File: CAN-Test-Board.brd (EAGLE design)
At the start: 52.3 x 59.4 mm, 52 parts, among them Y1 ECS-80-S-4X, Y2 ECS-80-S-4X

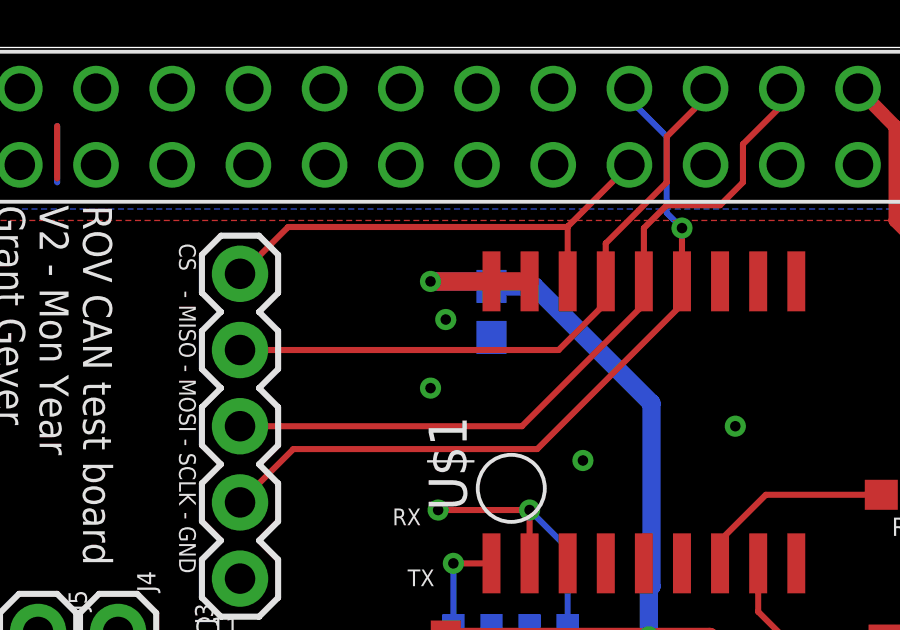
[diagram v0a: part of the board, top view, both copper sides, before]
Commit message: Add missing interrupt connection
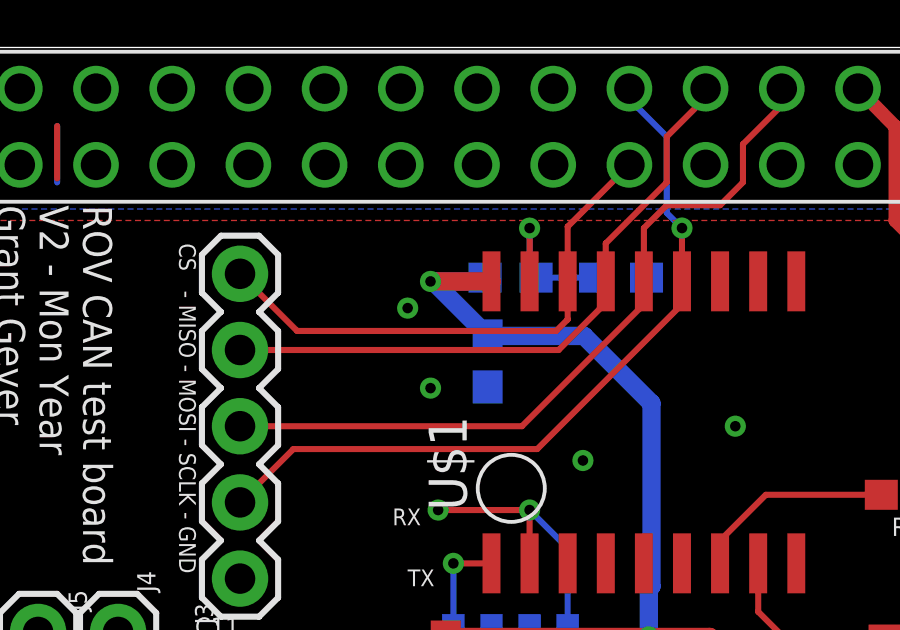
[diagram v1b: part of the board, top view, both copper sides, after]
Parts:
- added C19: 0.1uF, SparkFun-Capacitors:0603
- added R16: 10k, SparkFun-Resistors:0603
- C7: value 4.7uF -> 0.1uF
- R2: value 1k -> 10k
- moved C12 1.66 mm to (17.7, 48.9)
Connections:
- new net MCP_RESET: C19.2, R16.1, U$1.RESET
- net 3V3: now also R16.2; no longer U$1.RESET
- net GND: now also C19.1
- net INT: now also PCB1.P$37
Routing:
- net MCP_RESET: track 0.00 -> 5.50 mm, vias 0 -> 1
- net CS: track 16.3 -> 17.9 mm
- net 3V3: track 171.3 -> 171.9 mm
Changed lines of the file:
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@@
 <?xml version="1.0" encoding="utf-8"?>
 <!DOCTYPE eagle SYSTEM "eagle.dtd">
-<eagle version="9.6.2">
+<eagle version="9.6.0">
 <drawing>
 <settings>
@@
 <attribute name="VALUE" x="8.636" y="38.227" size="0.6096" layer="27" font="vector" ratio="20" align="top-center"/>
 </element>
-<element name="C12" library="SparkFun-Capacitors" library_urn="urn:adsk.eagle:library:510" package="0603" package3d_urn="urn:adsk.eagle:package:37414@1/1" value="0.1uF" x="17.78" y="50.546" smashed="yes" rot="MR90">
-<attribute name="NAME" x="18.542" y="50.546" size="0.6096" layer="26" font="vector" ratio="20" rot="MR90" align="bottom-center"/>
-<attribute name="PROD_ID" value="CAP-07885" x="-69.85" y="147.066" size="1.778" layer="28" rot="MR90" display="off"/>
-<attribute name="VALUE" x="17.018" y="50.546" size="0.6096" layer="28" font="vector" ratio="20" rot="MR90" align="top-center"/>
+<element name="C12" library="SparkFun-Capacitors" library_urn="urn:adsk.eagle:library:510" package="0603" package3d_urn="urn:adsk.eagle:package:37414@1/1" value="0.1uF" x="17.653" y="48.895" smashed="yes" rot="MR90">
+<attribute name="NAME" x="18.415" y="48.895" size="0.6096" layer="26" font="vector" ratio="20" rot="MR90" align="bottom-center"/>
+<attribute name="PROD_ID" value="CAP-07885" x="-69.977" y="145.415" size="1.778" layer="28" rot="MR90" display="off"/>
+<attribute name="VALUE" x="16.891" y="48.895" size="0.6096" layer="28" font="vector" ratio="20" rot="MR90" align="top-center"/>
 </element>
 <element name="C15" library="SparkFun-Capacitors" library_urn="urn:adsk.eagle:library:510" package="0603" package3d_urn="urn:adsk.eagle:package:37414@1/1" value="0.1uF" x="22.606" y="37.592" smashed="yes" rot="MR90">
@@
 <attribute name="VALUE" x="16.002" y="17.526" size="0.6096" layer="28" font="vector" ratio="20" rot="MR90" align="top-center"/>
 </element>
-<element name="C7" library="SparkFun-Capacitors" library_urn="urn:adsk.eagle:library:510" package="0603" package3d_urn="urn:adsk.eagle:package:37414@2/1" value="4.7uF" x="21.336" y="8.636" smashed="yes" rot="MR180">
+<element name="C7" library="SparkFun-Capacitors" library_urn="urn:adsk.eagle:library:510" package="0603" package3d_urn="urn:adsk.eagle:package:37414@2/1" value="0.1uF" x="21.336" y="8.636" smashed="yes" rot="MR180">
 <attribute name="NAME" x="21.336" y="7.874" size="0.6096" layer="26" font="vector" ratio="20" rot="MR180" align="bottom-center"/>
 <attribute name="PROD_ID" value="CAP-08280" x="98.806" y="96.266" size="1.778" layer="28" rot="MR180" display="off"/>
@@
 <attribute name="VALUE" x="31.75" y="40.386" size="0.6096" layer="27" font="vector" ratio="20" rot="R180" align="top-center"/>
 </element>
-<element name="R2" library="SparkFun-Resistors" library_urn="urn:adsk.eagle:library:532" package="0603" package3d_urn="urn:adsk.eagle:package:39650/1" value="1k" x="20.574" y="5.842" smashed="yes" rot="MR270">
+<element name="R2" library="SparkFun-Resistors" library_urn="urn:adsk.eagle:library:532" package="0603" package3d_urn="urn:adsk.eagle:package:39650/1" value="10k" x="20.574" y="5.842" smashed="yes" rot="MR270">
 <attribute name="NAME" x="19.812" y="5.842" size="0.6096" layer="26" font="vector" ratio="20" rot="MR270" align="bottom-center"/>
 <attribute name="PROD_ID" value="RES-07856" x="113.284" y="-28.448" size="1.778" layer="28" rot="MR270" display="off"/>
@@
 <attribute name="NAME" x="12.954" y="9.906" size="1.27" layer="25"/>
 <attribute name="VALUE" x="12.954" y="4.826" size="1.27" layer="27"/>
+</element>
+<element name="C19" library="SparkFun-Capacitors" library_urn="urn:adsk.eagle:library:510" package="0603" package3d_urn="urn:adsk.eagle:package:37414@1/1" value="0.1uF" x="22.098" y="51.689" smashed="yes" rot="MR0">
+<attribute name="NAME" x="22.098" y="52.451" size="0.6096" layer="26" font="vector" ratio="20" rot="MR0" align="bottom-center"/>
+<attribute name="PROD_ID" value="CAP-07885" x="22.098" y="51.689" size="1.778" layer="28" rot="MR0" display="off"/>
+<attribute name="VALUE" x="22.098" y="50.927" size="0.6096" layer="28" font="vector" ratio="20" rot="MR0" align="top-center"/>
+</element>
+<element name="R16" library="SparkFun-Resistors" library_urn="urn:adsk.eagle:library:532" package="0603" package3d_urn="urn:adsk.eagle:package:39650/1" value="10k" x="18.415" y="51.689" smashed="yes" rot="MR0">
+<attribute name="NAME" x="18.415" y="52.451" size="0.6096" layer="26" font="vector" ratio="20" rot="MR0" align="bottom-center"/>
+<attribute name="PROD_ID" value="RES-07856" x="18.288" y="51.689" size="1.778" layer="28" rot="MR0" display="off"/>
+<attribute name="VALUE" x="18.415" y="50.927" size="0.6096" layer="28" font="vector" ratio="20" rot="MR0" align="top-center"/>
 </element>
 </elements>
@@
 <via x="3.937" y="32.512" extent="1-16" drill="0.35"/>
 <via x="8.89" y="32.893" extent="1-16" drill="0.35"/>
-<via x="16.256" y="50.292" extent="1-16" drill="0.35"/>
+<via x="14.986" y="50.673" extent="1-16" drill="0.35"/>
 <via x="15.748" y="48.006" extent="1-16" drill="0.35"/>
 <via x="20.828" y="45.593" extent="1-16" drill="0.35"/>
@@
 <via x="37.338" y="53.086" extent="1-16" drill="0.35"/>
 <contactref element="RESET" pad="1"/>
+<contactref element="C19" pad="1"/>
 </signal>
 <signal name="CAN_H" class="1">
@@
 <wire x1="22.3774" y1="55.4482" x2="20.32" y2="53.3908" width="0.2032" layer="1"/>
 <wire x1="20.32" y1="53.3908" x2="20.32" y2="51.564" width="0.2032" layer="1"/>
-<wire x1="20.32" y1="53.3908" x2="20.306" y2="53.3768" width="0.2032" layer="1"/>
-<wire x1="9.44295" y1="51.816" x2="9.398" y2="51.816" width="0.2032" layer="1"/>
-<wire x1="11.00375" y1="53.3768" x2="9.44295" y2="51.816" width="0.2032" layer="1"/>
-<wire x1="20.306" y1="53.3768" x2="11.00375" y2="53.3768" width="0.2032" layer="1"/>
+<wire x1="9.398" y1="51.816" x2="11.303" y2="49.911" width="0.2032" layer="1"/>
+<wire x1="20.32" y1="50.292" x2="20.32" y2="51.564" width="0.2032" layer="1"/>
+<wire x1="11.303" y1="49.911" x2="19.939" y2="49.911" width="0.2032" layer="1"/>
+<wire x1="19.939" y1="49.911" x2="20.32" y2="50.292" width="0.2032" layer="1"/>
 </signal>
 <signal name="MISO" class="1">
@@
 <signal name="INT">
 <contactref element="U$1" pad="INT"/>
+<contactref element="PCB1" pad="P$37"/>
+<wire x1="4.5974" y1="57.9882" x2="25.4" y2="51.564" width="0" layer="19" extent="1-1"/>
 </signal>
 <signal name="3V3" class="2">
@@
 <wire x1="17.778" y1="51.562" x2="15.748" y2="51.562" width="0.6096" layer="1"/>
 <via x="15.748" y="51.562" extent="1-16" drill="0.35"/>
-<wire x1="15.748" y1="51.562" x2="17.614" y2="51.562" width="0.6096" layer="16"/>
-<wire x1="17.614" y1="51.562" x2="17.78" y2="51.396" width="0.6096" layer="16"/>
-<wire x1="17.78" y1="51.396" x2="19.216" y2="51.396" width="0.6096" layer="16"/>
-<wire x1="19.216" y1="51.396" x2="23.114" y2="47.498" width="0.6096" layer="16"/>
+<wire x1="15.748" y1="51.562" x2="15.836" y2="51.562" width="0.6096" layer="16"/>
+<wire x1="15.836" y1="51.562" x2="17.653" y2="49.745" width="0.6096" layer="16"/>
+<wire x1="17.653" y1="49.745" x2="20.867" y2="49.745" width="0.6096" layer="16"/>
+<wire x1="20.867" y1="49.745" x2="23.114" y2="47.498" width="0.6096" layer="16"/>
 <wire x1="23.026" y1="39.712" x2="25.058" y2="39.712" width="0.6096" layer="1"/>
 <wire x1="29.464" y1="35.306" x2="25.058" y2="39.712" width="0.6096" layer="1"/>
@@
 <wire x1="14.478" y1="39.624" x2="12.065" y2="37.211" width="0.6096" layer="1"/>
 <wire x1="9.652" y1="30.48" x2="2.286" y2="30.48" width="0.6096" layer="1"/>
-<contactref element="U$1" pad="RESET"/>
-<wire x1="17.78" y1="51.564" x2="19.05" y2="51.564" width="0.6096" layer="1"/>
+<contactref element="R16" pad="2"/>
+<wire x1="17.565" y1="51.689" x2="17.438" y2="51.562" width="0.6096" layer="16"/>
+<wire x1="17.438" y1="51.562" x2="15.748" y2="51.562" width="0.6096" layer="16"/>
 </signal>
 <signal name="N$3">
@@
 <wire x1="33.208" y1="51.628" x2="43.942" y2="51.628" width="0.4572" layer="1"/>
 </signal>
+<signal name="MCP_RESET">
+<contactref element="U$1" pad="RESET"/>
+<contactref element="R16" pad="1"/>
+<contactref element="C19" pad="2"/>
+<wire x1="21.248" y1="51.689" x2="19.265" y2="51.689" width="0.2032" layer="16"/>
+<wire x1="19.05" y1="51.564" x2="19.05" y2="53.34" width="0.2032" layer="1"/>
+<via x="19.05" y="53.34" extent="1-16" drill="0.35"/>
+<wire x1="19.265" y1="51.689" x2="19.05" y2="51.904" width="0.2032" layer="16"/>
+<wire x1="19.05" y1="51.904" x2="19.05" y2="53.34" width="0.2032" layer="16"/>
+</signal>
 </signals>

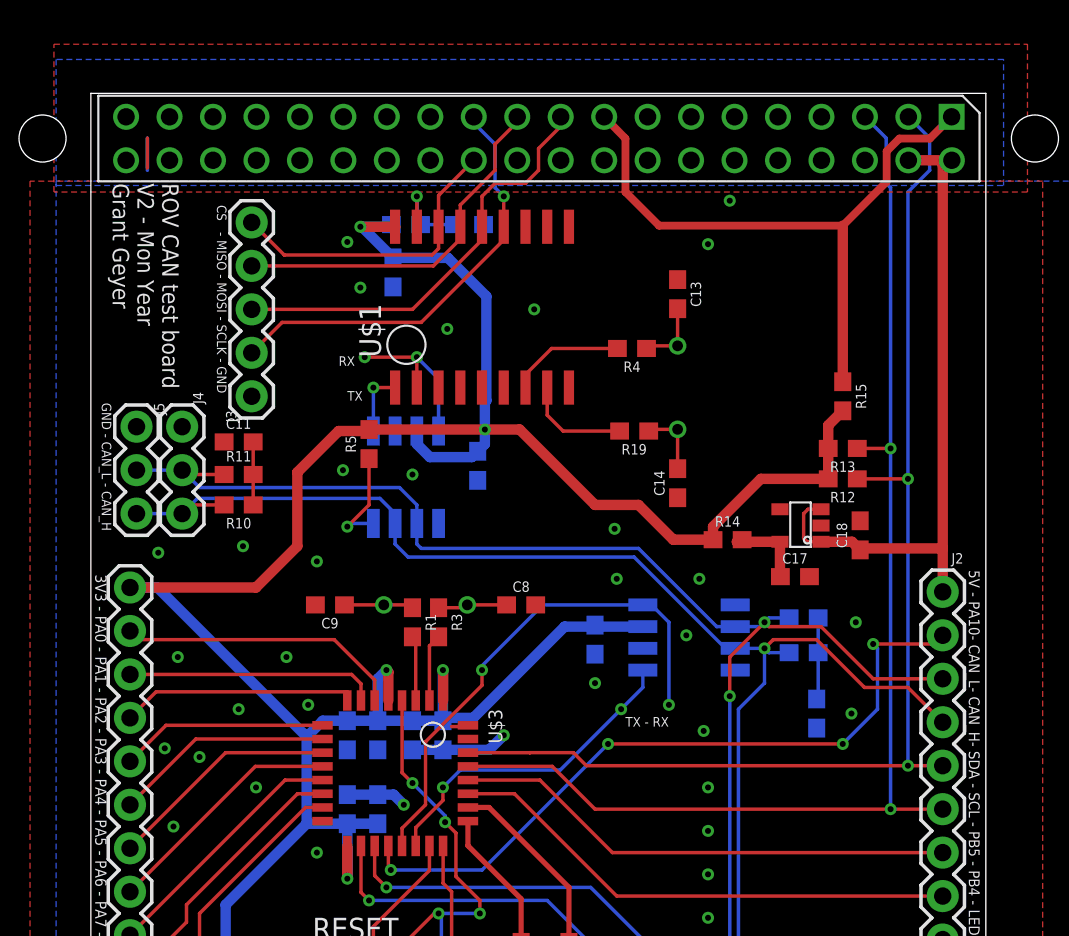
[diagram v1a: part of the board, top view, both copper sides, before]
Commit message: Update parts and values. Fix missing connection?
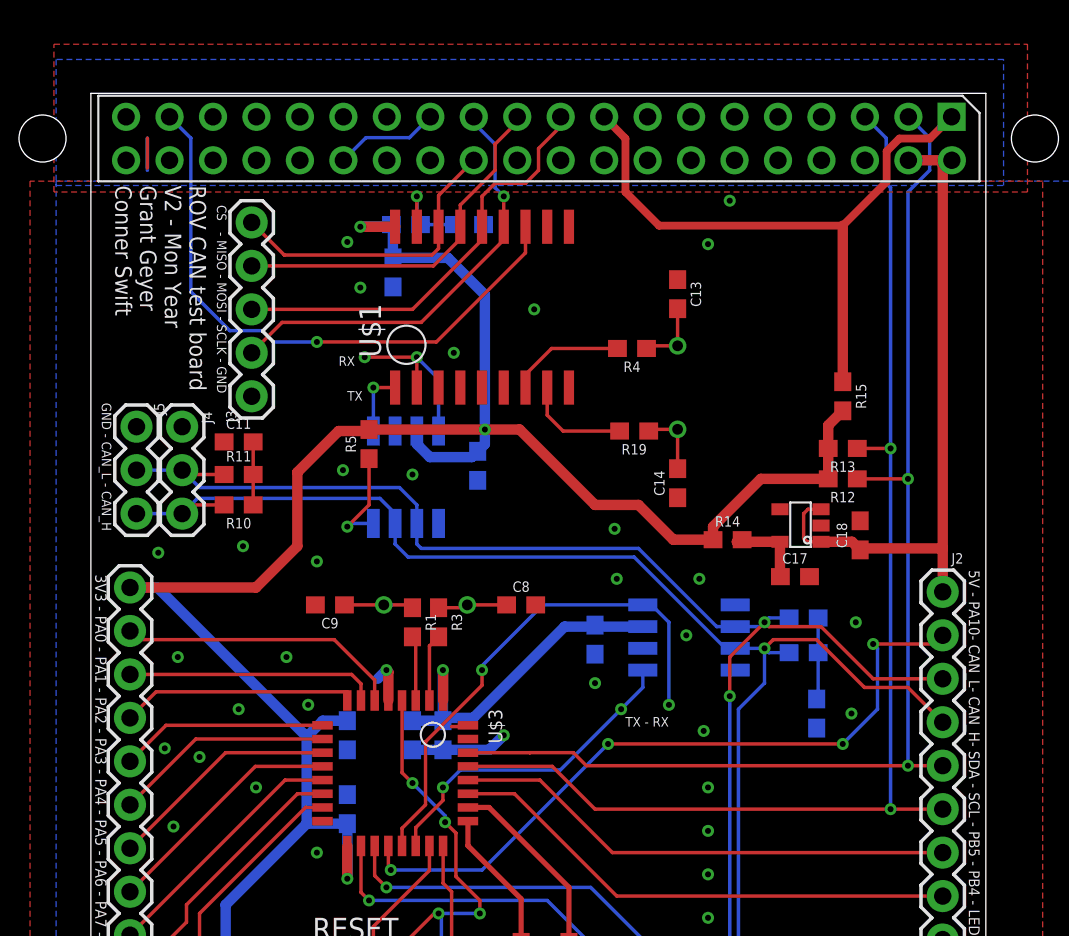
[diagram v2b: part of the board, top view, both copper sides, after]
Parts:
- removed C4, C6: 4.7uF, SparkFun-Capacitors:0603
- C10, C2, C3, C5: value 4.7uF -> 0.1uF
- C8, C9: value 4.7uF -> 18pF
- PCB1: value RPI2 -> RPI4; device MicrocontrollerComponents:RPI2 -> AUX, RaspberryPi:RPI4
- R1, R3: value 1k -> 0
- U$1: device PI_Shield_Library:MCP2515 -> IC, STM and CAN parts:SOIC-18
- U$2, U$8: device PI_Shield_Library:TCAN337D -> IC, STM and CAN parts:SOIC-8
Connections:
- net N$3 renamed OSC_2_MID
- net N$4 renamed OSC_1_MID
- removed net N$6: R5.1, U$2.S
- new net RX_CAN_INT0: U$1.11
- new net RX_CAN_INT1: U$1.10
- new net SILENT_PI: R5.1, U$2.8
- net 3V3: now also U$1.18, U$2.3, U$8.3; no longer C4.1, C6.1, U$1.VDD, U$2.VCC, U$8.VCC
- net 3V3_PI: now also PCB1.1, PCB1.17; no longer PCB1.P$1, PCB1.P$17
- net 5V: now also PCB1.2, PCB1.4; no longer PCB1.P$2, PCB1.P$4
- net CAN_H: now also U$2.7, U$8.7; no longer U$2.CANH, U$8.CANH
- net CAN_L: now also U$2.6, U$8.6; no longer U$2.CANL, U$8.CANL
- net CAN_RX_PI: now also U$1.2, U$2.4; no longer U$1.RXCAN, U$2.RXD
- net CAN_RX_STM: now also U$8.4; no longer U$8.RXD
- net CAN_TX_PI: now also U$1.1, U$2.1; no longer U$1.TXCAN, U$2.TXD
- net CAN_TX_STM: now also U$8.1; no longer U$8.TXD
- net CS: now also PCB1.24, U$1.16; no longer PCB1.P$24, U$1.CS
- net FAULT: now also U$2.5; no longer U$2.FAULT
- net GND: now also PCB1.14, PCB1.20, PCB1.25, PCB1.30, PCB1.34, PCB1.39, PCB1.6, PCB1.9, U$1.9, U$2.2, U$8.2; no longer C4.2, C6.2, PCB1.P$14, PCB1.P$20, PCB1.P$25, PCB1.P$30, PCB1.P$34, PCB1.P$39, PCB1.P$6, PCB1.P$9, U$1.VSS, U$2.GND, U$8.GND
- net INT: now also PCB1.37, U$1.12; no longer PCB1.P$37, U$1.INT
- net MCP_RESET: now also U$1.17; no longer U$1.RESET
- net MISO: now also PCB1.21, U$1.15; no longer PCB1.P$21, U$1.SO
- net MOSI: now also PCB1.19, U$1.14; no longer PCB1.P$19, U$1.SI
- net OSC1: now also U$1.8; no longer U$1.OSC1
- net OSC2: now also U$1.7; no longer U$1.OSC2
- net SCL: now also PCB1.5; no longer PCB1.P$5
- net SCLK: now also PCB1.23, U$1.13; no longer PCB1.P$23, U$1.SCK
- net SDA: now also PCB1.3; no longer PCB1.P$3
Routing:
- net INT: track 0.00 -> 35.2 mm, vias 0 -> 1
- net 3V3: track 171.9 -> 163.2 mm
- net SILENT_PI: track 0.00 -> 6.10 mm, vias 0 -> 1
- net N$6: track 6.10 -> 0.00 mm, vias 1 -> 0
- net GND: track 13.9 -> 16.4 mm, vias 40 -> 39
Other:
- board text added: "ROV CAN test board V2 - Mon Year Grant Geyer Conner Swift"
- board text removed: "ROV CAN test board V2 - Mon Year Grant Geyer"
